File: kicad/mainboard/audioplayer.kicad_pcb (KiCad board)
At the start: 4 copper layers, 100.3 x 99.7 mm, 151 parts, among them IC1 XC6193BANNER-G, J1 Micro_SD_Card, J2 USB_B, J3 L, J4 R, J5 CHG, Q1 DMN2020LSN, Q2 SSM3J332R, SW1 VOL-, SW2 LEFT, SW3 MID, SW4 RIGHT, SW5 VOL+, U1 RC-552, U10 NCP115, U11 TPS63001, U2 UMH4NTN, U4 CP2102N-A02-GQFN24, U5 MCP73831-2-OT, U6 PAM8408, U7 VS1053b, U8 MT3608, Y1 12.288MHz

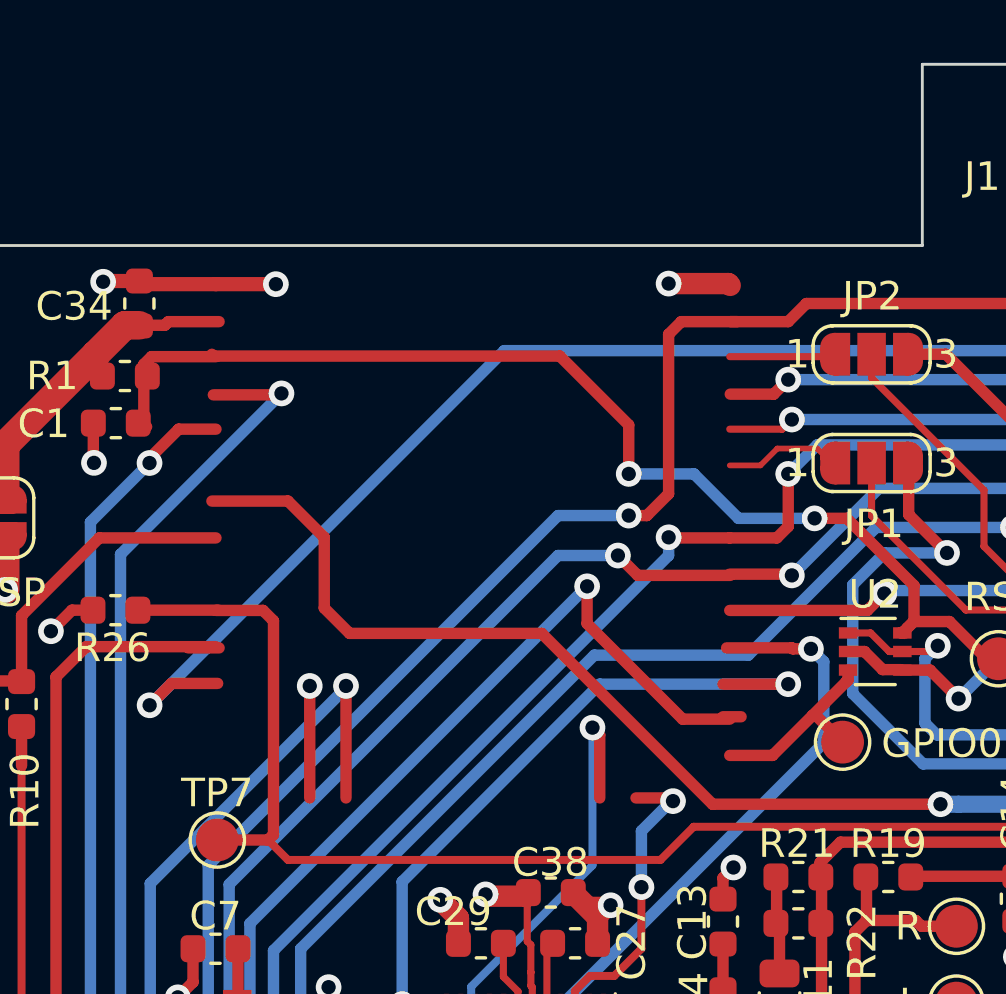
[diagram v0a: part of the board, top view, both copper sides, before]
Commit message: display FX, audio glitches
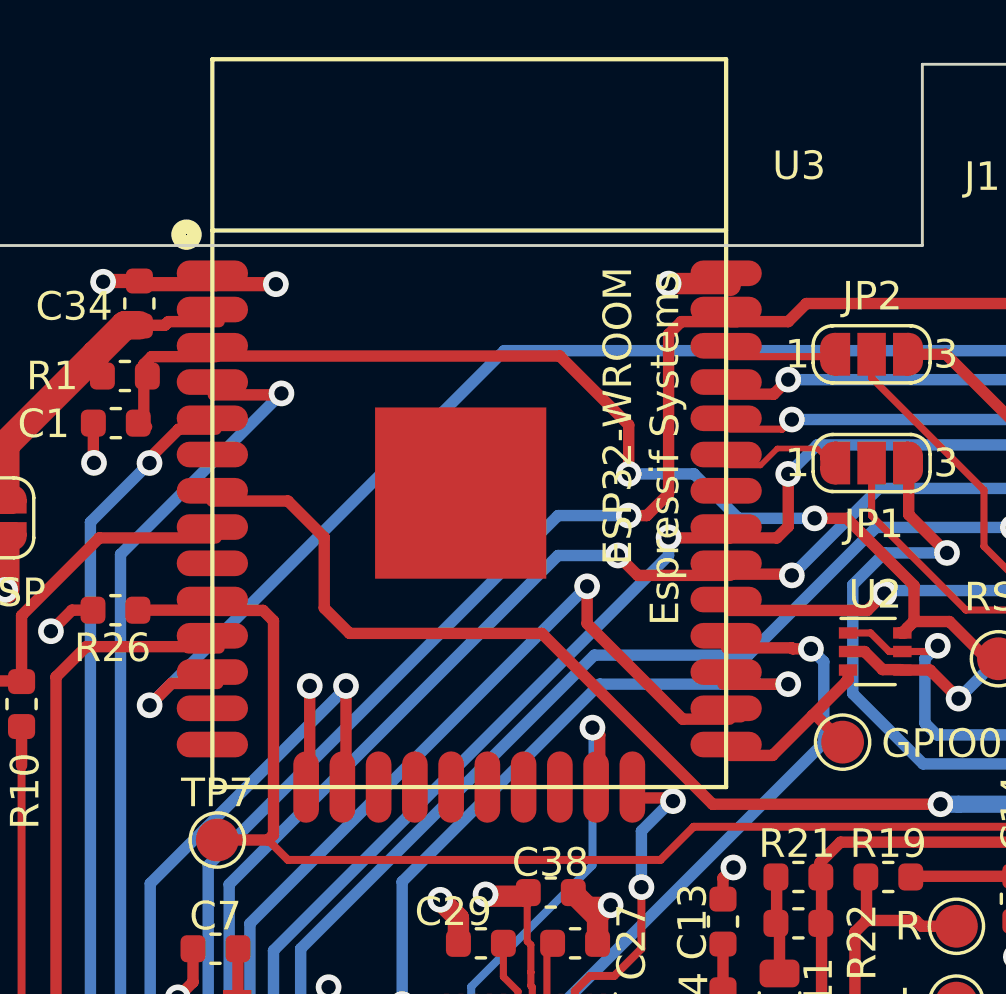
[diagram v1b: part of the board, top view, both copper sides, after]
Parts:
- added U3: ESP-WROOM32, audioplayer:ESP32-WROOM, F.Cu at (81.9, 34.2)
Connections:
- D8 pad 2: (no net) -> Net-(D8-Pad2)
- J1 pad 1: (no net) -> Net-(J1-Pad1)
- J1 pad 8: (no net) -> Net-(J1-Pad8)
- U4 pad 1: (no net) -> Net-(U4-Pad1)
- U4 pad 10: (no net) -> Net-(U4-Pad10)
- U4 pad 11: (no net) -> Net-(U4-Pad11)
- U4 pad 12: (no net) -> Net-(U4-Pad12)
- U4 pad 15: (no net) -> Net-(U4-Pad15)
- U4 pad 16: (no net) -> Net-(U4-Pad16)
- U4 pad 17: (no net) -> Net-(U4-Pad17)
- U4 pad 18: (no net) -> Net-(U4-Pad18)
- U4 pad 22: (no net) -> Net-(U4-Pad22)
- U4 pad 24: (no net) -> Net-(U4-Pad24)
- U7 pad 1: (no net) -> Net-(U7-Pad1)
- U7 pad 15: (no net) -> Net-(U7-Pad15)
- U7 pad 2: (no net) -> Net-(U7-Pad2)
- U7 pad 27: (no net) -> Net-(U7-Pad27)
- U7 pad 48: (no net) -> Net-(U7-Pad48)
- U8 pad 6: (no net) -> Net-(U8-Pad6)
